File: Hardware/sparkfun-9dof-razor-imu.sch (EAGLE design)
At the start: 57 parts, among them J1 LiPo, J3 USD_CONNECTOR, U1 3.3V, U2 MCP73831, U3 MPU-9250, U4 ATSAMD21G-A, Y1 32.768kHz

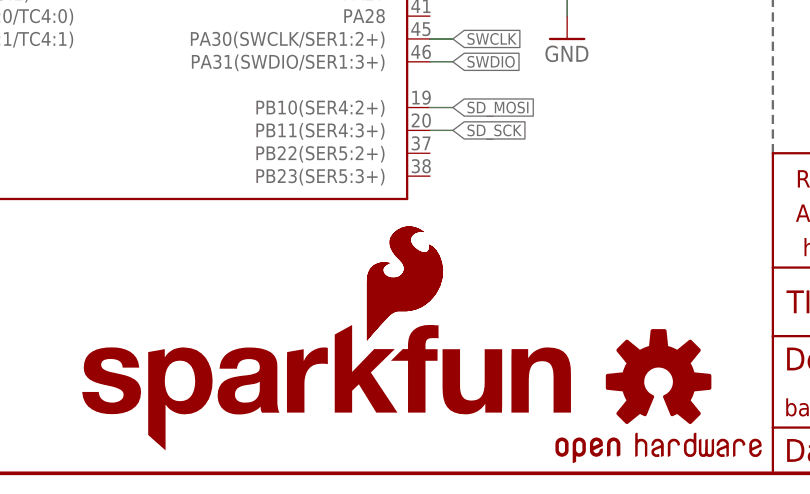
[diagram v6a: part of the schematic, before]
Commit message: Checklist adjustments - mostly silkscreen nudging.
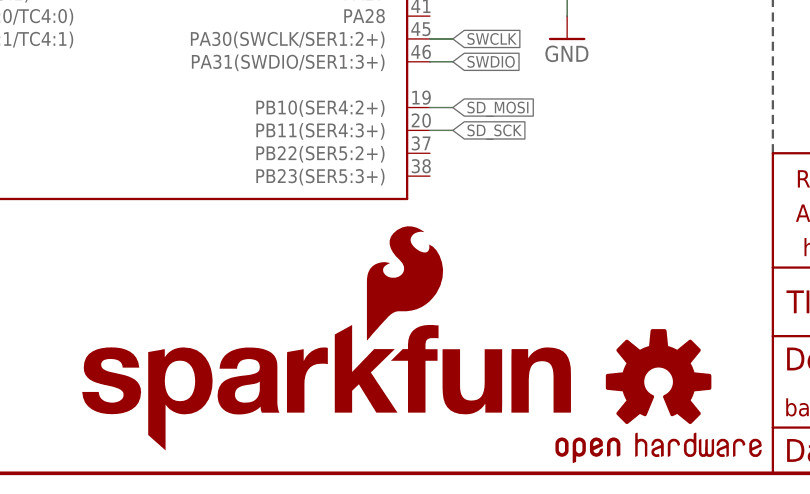
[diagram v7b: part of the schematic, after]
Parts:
- removed LOGO4: SFE_LOGO_FLAME.1_INCH, SparkFun-Aesthetics:SFE_LOGO_FLAME.1_INCH
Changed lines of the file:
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@@
 <part name="TP1" library="SparkFun-Connectors" deviceset="TEST-POINT" device="3" value="TEST-POINT3"/>
 <part name="TP2" library="SparkFun-Connectors" deviceset="TEST-POINT" device="3" value="TEST-POINT3"/>
-<part name="LOGO4" library="SparkFun-Aesthetics" deviceset="SFE_LOGO_FLAME" device=".1_INCH"/>
 </parts>
 <sheets>
@@
 <instance part="TP1" gate="G$1" x="17.78" y="38.1" rot="MR0"/>
 <instance part="TP2" gate="G$1" x="17.78" y="33.02" rot="MR0"/>
-<instance part="LOGO4" gate="G$1" x="101.854" y="14.224"/>
 </instances>
 <busses>

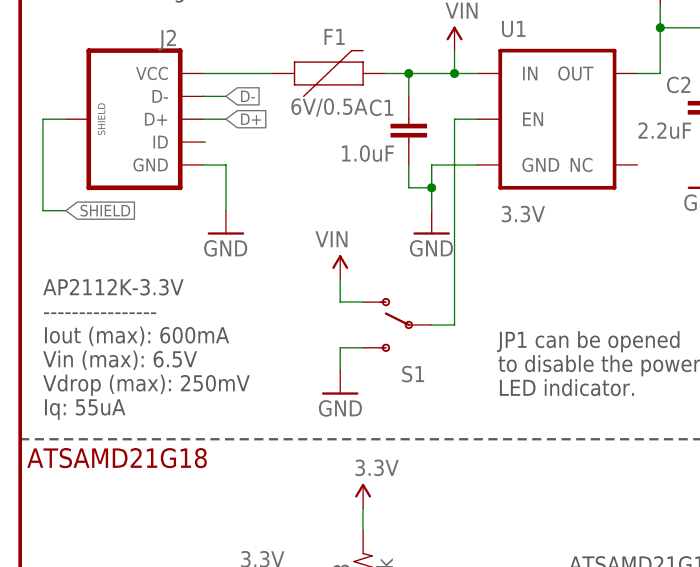
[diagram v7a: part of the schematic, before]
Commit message: Value Added to .brd File
Right Angle Slide Switch Added for 3D Modeling
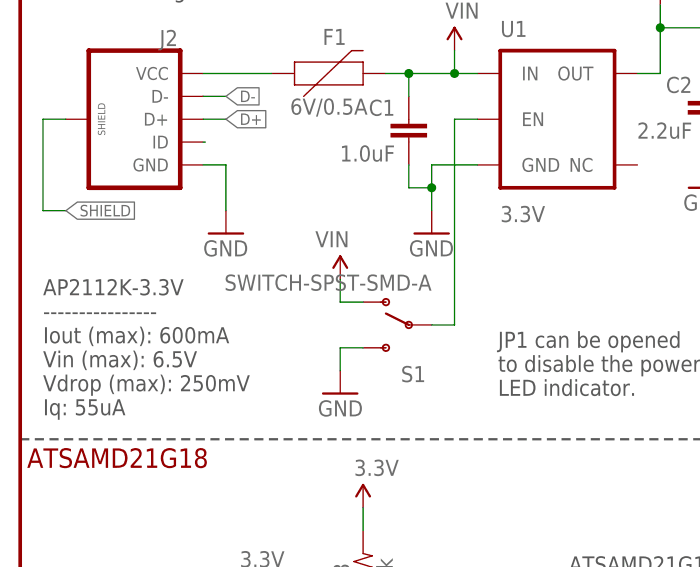
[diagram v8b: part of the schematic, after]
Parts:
- S1: value (none) -> SWITCH-SPST-SMD-A
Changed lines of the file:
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@@
 <?xml version="1.0" encoding="utf-8"?>
 <!DOCTYPE eagle SYSTEM "eagle.dtd">
-<eagle version="7.5.0">
+<eagle version="7.7.0">
 <drawing>
 <settings>
@@
 <part name="H4" library="SparkFun-Electromechanical" deviceset="STAND-OFF" device=""/>
 <part name="H3" library="SparkFun-Electromechanical" deviceset="STAND-OFF" device=""/>
-<part name="S1" library="SparkFun-Electromechanical" deviceset="SWITCH-SPDT" device="-SMD-A"/>
+<part name="S1" library="SparkFun-Electromechanical" deviceset="SWITCH-SPDT" device="-SMD-A" value="SWITCH-SPST-SMD-A"/>
 <part name="SUPPLY10" library="SparkFun-PowerSymbols" deviceset="3.3V" device=""/>
 <part name="SUPPLY7" library="SparkFun-PowerSymbols" deviceset="3.3V" device=""/>
